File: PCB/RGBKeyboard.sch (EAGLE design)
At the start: 1 part, among them U1 MSP430F5529_PN_80

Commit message: USB lib and schematic
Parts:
- added C10, C11: 10 pF, rcl:C-USC0603K
- added C12: 4.7 uF, rcl:C-USC0603K
- added C4, C5: 32 pF, rcl:C-USC0603K
- added C6, C7: 220 nF, rcl:C-USC0603K
- added C8: 100 nF, rcl:C-USC0603K
- added C9: 10 uF, rcl:C-USC0603K
- added D2: BAS40, diode:BAS40
- added P2: 0475890001, MICRO_USB_B:0475890001
- added R5, R6, R7, R8: 27, rcl:R-US_R0603
- added R9: 1 M, rcl:R-US_R0603
- added S1: PTS645SM43SMTR, PTS645SM43SMTR:PTS645SM43SMTR
- added Y1: ECS-40-20-5PX-TR, ECS-40-20-5PX-TR:ECS-40-20-5PX-TR
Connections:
- removed net PU.0/DM: U1.PU.0/DP
- new net GND: C10.2, C11.2, C12.2, C4.2, C5.2, P2.GND, R9.1
- new net N$10: D2.C, P2.VCC
- new net N$4: R5.2, S1.P$1
- new net N$5: C8.2
- new net N$7: P2.ID
- new net N$8: P2.D-, R6.2
- new net N$9: P2.D+, R7.2
- new net PU.0/DP: C10.1, R7.1, R8.2, R9.2, U1.PU.0/DP
- new net V18: C7.1, U1.V18
- new net VBUS: C12.1, D2.A, U1.VBUS
- new net VSSU: C6.2, C7.2, C9.2, U1.VSSU
- new net VUSB: C6.1, C8.1, C9.1, S1.P$2, U1.VUSB
- new net XT2IN: C5.1, U1.P5.2/XT2IN, Y1.1
- new net XT2OUT: C4.1, U1.P5.3/XT2OUT, Y1.2
- net PU.1/DM: now also C11.1, R6.1
- net PUR: now also R5.1, R8.1

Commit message: Switches with LEDs and diodes
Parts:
- added D1, D10, D11, D12, D13, D3, D4, D5, D6, D7, D8, D9: BAV21W-7-F, BAV21W-7-F:BAV21W-7-F
- added U$1, U$10, U$11, U$12, U$2, U$3, U$4, U$5, U$6, U$7, U$8, U$9: CHERRY_MXCHERRY_MX_LED, CHERRY_MX:CHERRY_MXCHERRY_MX_LED
- added U10, U11, U12, U13, U2, U3, U4, U5, U6, U7, U8, U9: 3341, 3341:3341
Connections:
- new net +3V3: U10.VDD, U11.VDD, U12.VDD, U13.VDD, U2.VDD, U3.VDD, U4.VDD, U5.VDD, U6.VDD, U7.VDD, U8.VDD, U9.VDD
- new net CKO0: U5.CKO, U6.CKI
- new net CKO1: U10.CKI, U9.CKO
- new net COL0: U$1.2, U$3.2, U$9.2
- new net COL1: U$10.2, U$2.2, U$4.2
- new net COL2: U$11.2, U$5.2, U$7.2
- new net COL3: U$12.2, U$6.2, U$8.2
- new net N$1: D9.A, U$8.1
- new net N$11: D11.A, U$10.1
- new net N$12: D13.A, U$12.1
- new net N$13: U2.CKO, U3.CKI
- new net N$14: U2.SDO, U3.SDI
- new net N$15: U3.CKO, U4.CKI
- new net N$16: U3.SDO, U4.SDI
- new net N$17: U4.CKO, U5.CKI
- new net N$18: U4.SDO, U5.SDI
- new net N$19: U6.CKO, U7.CKI
- new net N$2: D5.A, U$4.1
- new net N$20: U6.SDO, U7.SDI
- new net N$21: U7.CKO, U8.CKI
- new net N$22: U7.SDO, U8.SDI
- new net N$23: U8.CKO, U9.CKI
- new net N$24: U8.SDO, U9.SDI
- new net N$25: U10.CKO, U11.CKI
- new net N$26: U10.SDO, U11.SDI
- new net N$27: U11.CKO, U12.CKI
- new net N$28: U11.SDO, U12.SDI
- new net N$29: U12.CKO, U13.CKI
- new net N$3: D7.A, U$6.1
- new net N$30: U12.SDO, U13.SDI
- new net N$6: D3.A, U$2.1
- new net ROW0: D1.A, D1.C, D3.C, D6.A, D6.C, D7.C, U$1.1, U$5.1
- new net ROW1: D4.A, D4.C, D5.C, D8.A, D8.C, D9.C, U$3.1, U$7.1
- new net ROW2: D10.A, D10.C, D11.C, D12.A, D12.C, D13.C, U$11.1, U$9.1
- new net SDO0: U5.SDO, U6.SDI
- new net SDO1: U10.SDI, U9.SDO
- new net UCA0CLK: U2.CKI
- new net UCA0SIMO: U2.SDI
- net GND: now also U10.GND, U11.GND, U12.GND, U13.GND, U2.GND, U3.GND, U4.GND, U5.GND, U6.GND, U7.GND, U8.GND, U9.GND

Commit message: Double check power and add headers
Power is sourced from USB through VBUS, goes through
internal LDO to VUSB and goes to DVCC.

Headers are for row/col debug and Spi-By-Wire
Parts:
- removed U$12: CHERRY_MXCHERRY_MX_LED, CHERRY_MX:CHERRY_MXCHERRY_MX_LED
- added C1, C2: 10 uF, rcl:C-USC0603K
- added C13: 470 nF, rcl:C-USC0603K
- added C14, C15, C3: 100 nF, rcl:C-USC0603K
- added D14: BAV21W-7-F, BAV21W-7-F:BAV21W-7-F
- added R1, R2, R3, R4: 4.7k, rcl:R-US_R0603
- added R10: 47 k, rcl:R-US_R0603
- added SV1, SV3: (no value), con-lstb:MA04-1
- added SV2: (no value), con-lstb:MA03-1
- added U$13: CHERRY_MX_LED, CHERRY_MX:CHERRY_MX_LED
- U$1, U$2, U$3, U$4, U$5, U$6, U$7, U$8, U$9: value CHERRY_MXCHERRY_MX_LED -> CHERRY_MX_LED; device CHERRY_MX:CHERRY_MXCHERRY_MX_LED -> CHERRY_MX:CHERRY_MX_LED
- U$10: value CHERRY_MXCHERRY_MX_LED -> CHERRY_MX_LEDCHERRY_MX_LED_1_2; device CHERRY_MX:CHERRY_MXCHERRY_MX_LED -> CHERRY_MX:CHERRY_MX_LEDCHERRY_MX_LED_1_2
- U$11: value CHERRY_MXCHERRY_MX_LED -> CHERRY_MX_LEDCHERRY_MX_LED_1_6; device CHERRY_MX:CHERRY_MXCHERRY_MX_LED -> CHERRY_MX:CHERRY_MX_LEDCHERRY_MX_LED_1_6
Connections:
- new net DVCC: C1.1, C14.1, C15.1, C2.1, C3.1, R10.1, U1.AVCC1, U1.DVCC1, U1.DVCC2, U1.VUSB
- new net N$31: C13.1, U1.VCORE
- new net N$32: D14.A, SV1.4
- new net N$33: U$3.2, U$4.2
- new net N$34: R10.2, U1.*RST/NMI/SBWTDIO
- new net N$35: U$7.2, U$8.2
- new net N$36: U$10.2, U$11.2
- new net RST: SV1.3
- new net TST: SV1.2
- net COL0: now also R1.2, SV3.4, U$13.2, U$2.2, U1.P1.3/TA0.2; no longer U$3.2, U$9.2
- net COL1: now also R2.2, SV3.3, U$5.2, U1.P1.4/TA0.3; no longer U$10.2, U$2.2
- net COL2: now also R3.2, SV3.2, U$6.2, U1.P1.5/TA0.4; no longer U$11.2, U$5.2
- net COL3: now also R4.2, SV3.1, U$10.2, U$9.2, U1.P1.6/TA1CLK/CBOUT; no longer U$12.2, U$6.2, U$8.2
- net GND: now also C1.2, C13.2, C14.2, C15.2, C2.2, C3.2, R1.1, R2.1, R3.1, R4.1, SV1.1, U1.AVSS1, U1.AVSS2, U1.DVSS1, U1.DVSS2
- net N$1: now also U$10.1; no longer U$8.1
- net N$10: now also D2.A; no longer D2.C
- net N$11: now also U$3.1; no longer U$10.1
- net N$12: now also U$11.1; no longer U$12.1
- net N$3: now also U$9.1; no longer U$6.1
- net N$6: now also U$5.1; no longer U$2.1
- net ROW0: now also SV2.3, U$13.1, U$6.1, U1.P1.0/TA0CLK/ACLK; no longer U$1.1, U$5.1
- net ROW1: now also SV2.2, U$1.1, U1.P1.1/TA0.0; no longer U$3.1
- net ROW2: now also SV2.1, U$2.1, U$8.1, U1.P1.2/TA0.1; no longer U$11.1, U$9.1
- net VBUS: now also D14.C, D2.C; no longer D2.A
- net VUSB: no longer U1.VUSB
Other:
- moved on the sheet: D2

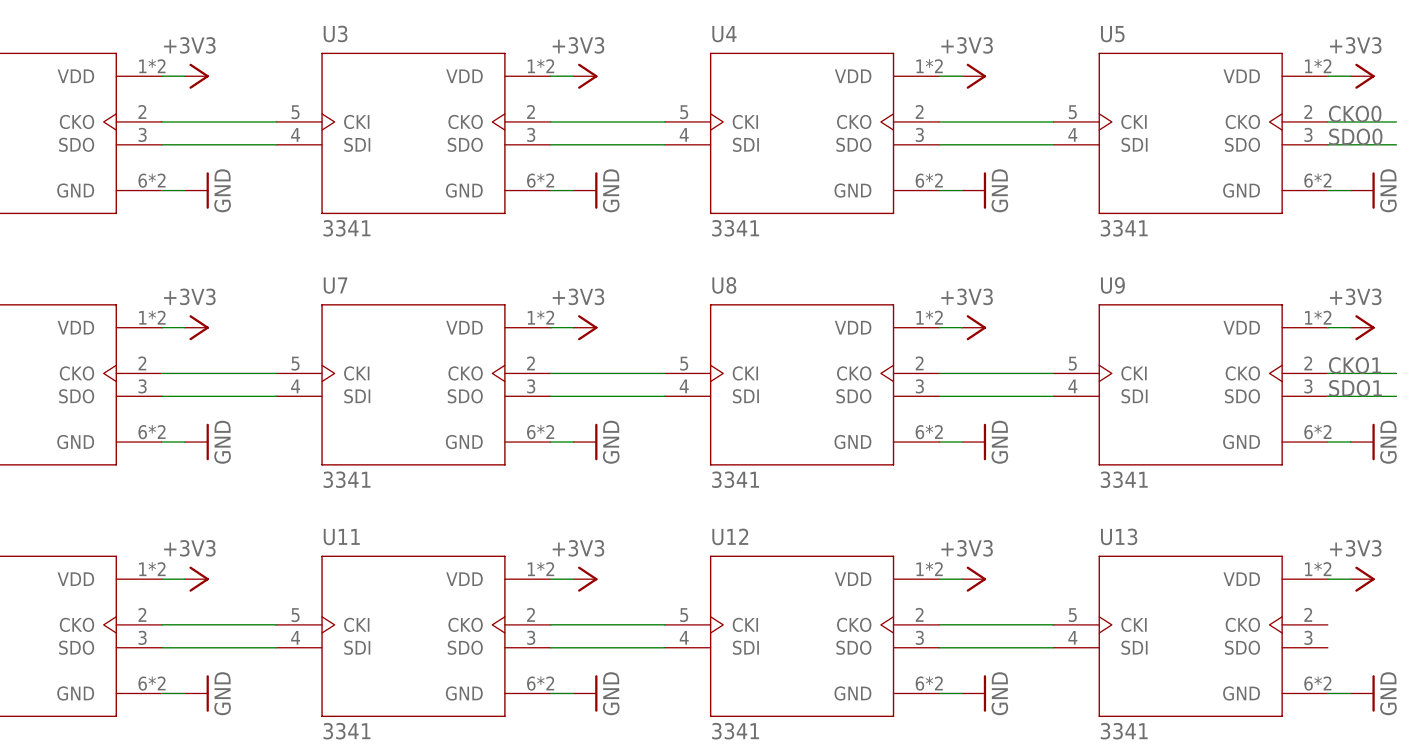
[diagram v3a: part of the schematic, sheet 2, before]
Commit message: Add power debug pins and double check connections
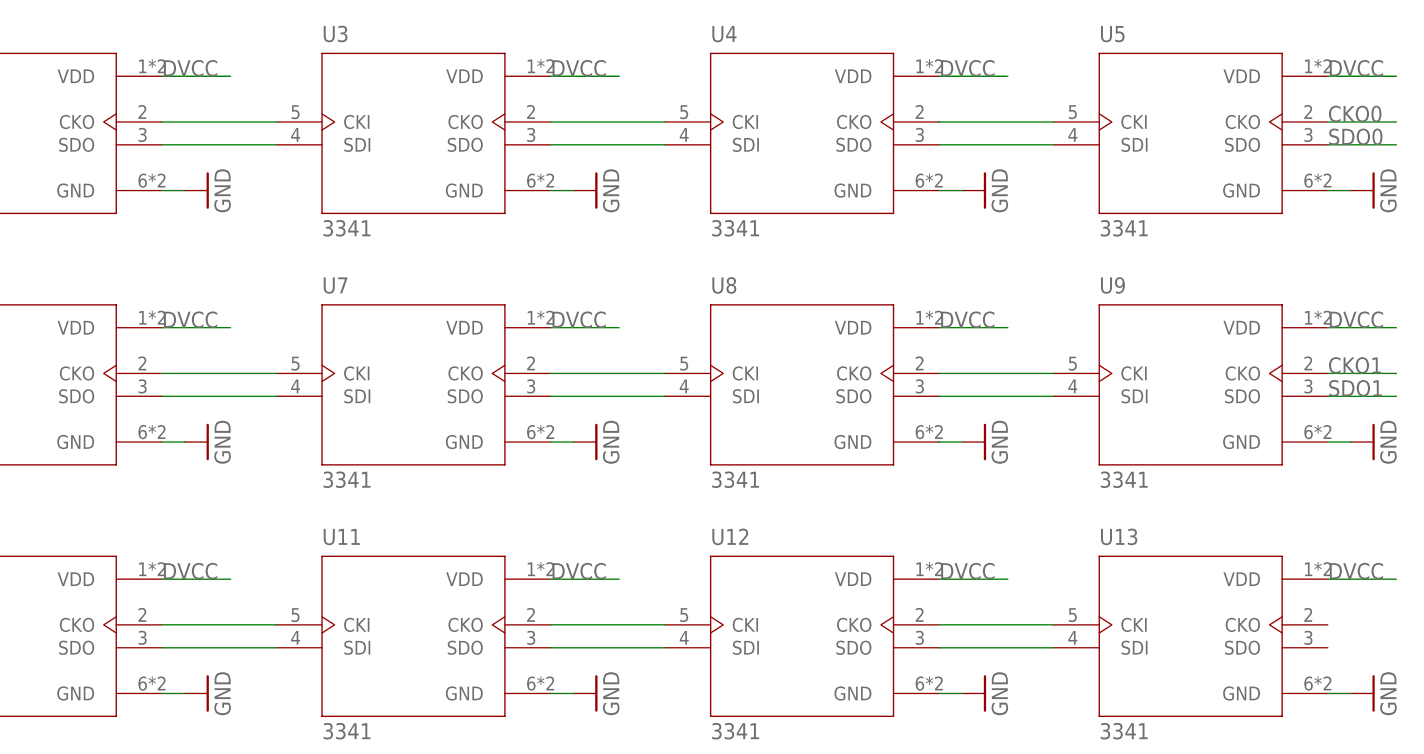
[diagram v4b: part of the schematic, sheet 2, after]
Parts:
- added SV4: (no value), con-lstb:MA03-1
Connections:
- removed net +3V3: U10.VDD, U11.VDD, U12.VDD, U13.VDD, U2.VDD, U3.VDD, U4.VDD, U5.VDD, U6.VDD, U7.VDD, U8.VDD, U9.VDD
- net DVCC: now also SV4.3, U10.VDD, U11.VDD, U12.VDD, U13.VDD, U2.VDD, U3.VDD, U4.VDD, U5.VDD, U6.VDD, U7.VDD, U8.VDD, U9.VDD
- net GND: now also SV4.2
- net UCA0CLK: now also U1.P2.7/UCB0STE/UCA0CLK
- net UCA0SIMO: now also U1.P3.3/UCA0TXD/UCA0SIMO

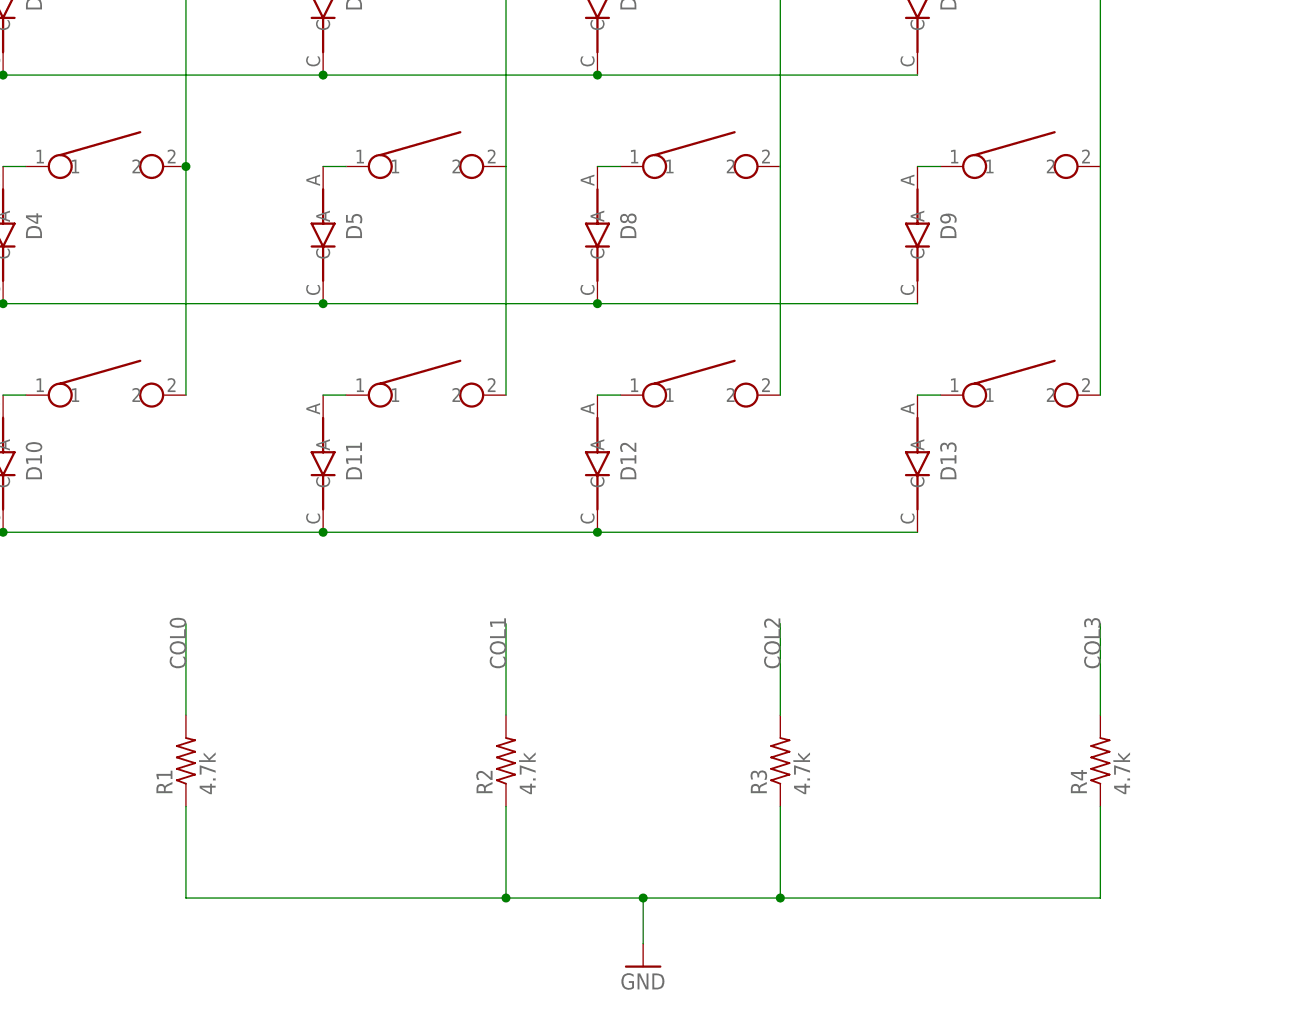
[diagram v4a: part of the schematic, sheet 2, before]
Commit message: Temp board and schematic (commit for progress)
Will be switching to a simpler design using the MSP430F5529
launchpad because the tools I have right now make it hard to
solder the MSP430 onto the board. Instead, the launchpad will
be connected to the board using header pins.
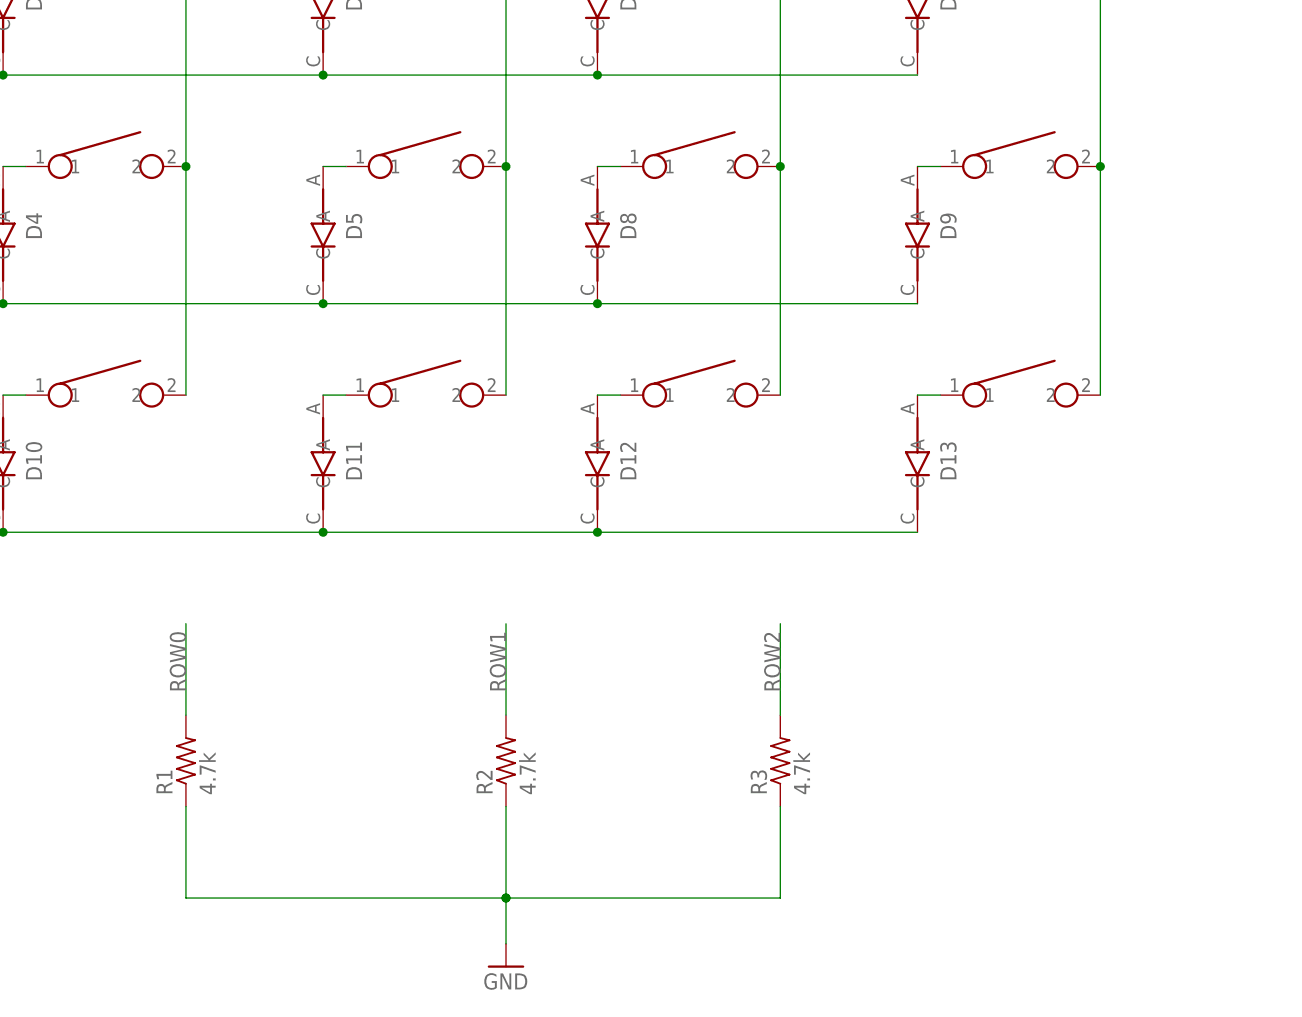
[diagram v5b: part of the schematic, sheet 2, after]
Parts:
- removed R4: 4.7k, rcl:R-US_R0603
- removed U$13: CHERRY_MX_LED, CHERRY_MX:CHERRY_MX_LED
- added U$12: CHERRY_MX, CHERRY_MX:CHERRY_MX
- R5: value 27 -> 100
- U$1, U$2, U$3, U$4, U$5, U$6, U$7, U$8, U$9: value CHERRY_MX_LED -> CHERRY_MX; device CHERRY_MX:CHERRY_MX_LED -> CHERRY_MX:CHERRY_MX
- U$10: value CHERRY_MX_LEDCHERRY_MX_LED_1_2 -> CHERRY_MXCHERRY_MX_1_2; device CHERRY_MX:CHERRY_MX_LEDCHERRY_MX_LED_1_2 -> CHERRY_MX:CHERRY_MXCHERRY_MX_1_2
- U$11: value CHERRY_MX_LEDCHERRY_MX_LED_1_6 -> CHERRY_MXCHERRY_MX_1_6; device CHERRY_MX:CHERRY_MX_LEDCHERRY_MX_LED_1_6 -> CHERRY_MX:CHERRY_MXCHERRY_MX_1_6
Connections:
- removed net N$34: R10.2, U1.*RST/NMI/SBWTDIO
- new net N$37: D10.A, U$3.1
- new net N$38: D1.A, U$1.1
- new net N$39: D4.A, U$2.1
- net COL0: now also U$3.2, U1.P1.6/TA1CLK/CBOUT; no longer R1.2, U$13.2, U1.P1.3/TA0.2
- net COL1: now also U$6.2, U1.P1.5/TA0.4; no longer R2.2, U1.P1.4/TA0.3
- net COL2: now also U$8.2, U$9.2, U1.P1.4/TA0.3; no longer R3.2, U$6.2, U1.P1.5/TA0.4
- net COL3: now also U$11.2, U$12.2, U1.P1.3/TA0.2; no longer R4.2, U$9.2, U1.P1.6/TA1CLK/CBOUT
- net GND: no longer R4.1
- net N$11: now also U$6.1; no longer U$3.1
- net N$2: now also U$5.1; no longer U$4.1
- net N$3: now also U$12.1; no longer U$9.1
- net N$33: now also D6.A, U$7.1; no longer U$3.2, U$4.2
- net N$35: now also D8.A, U$8.1; no longer U$7.2, U$8.2
- net N$36: now also D12.A, U$9.1; no longer U$10.2, U$11.2
- net N$6: now also U$4.1; no longer U$5.1
- net ROW0: now also R1.2, U1.P1.2/TA0.1; no longer D1.A, D6.A, U$13.1, U$6.1, U1.P1.0/TA0CLK/ACLK
- net ROW1: now also R2.2; no longer D4.A, D8.A, U$1.1, U$7.1
- net ROW2: now also R3.2, U1.P1.0/TA0CLK/ACLK; no longer D10.A, D12.A, U$2.1, U$8.1, U1.P1.2/TA0.1
- net RST: now also R10.2, U1.*RST/NMI/SBWTDIO

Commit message: Have a decent prototype but may switch LEDs
WS2812-2020s seem easier to solder but are harder to control.
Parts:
- removed C1, C2, C9: 10 uF, rcl:C-USC0603K
- removed C10, C11: 10 pF, rcl:C-USC0603K
- removed C12: 4.7 uF, rcl:C-USC0603K
- removed C13: 470 nF, rcl:C-USC0603K
- removed C14, C15, C3, C8: 100 nF, rcl:C-USC0603K
- removed C4, C5: 32 pF, rcl:C-USC0603K
- removed C6, C7: 220 nF, rcl:C-USC0603K
- removed P2: 0475890001, MICRO_USB_B:0475890001
- removed R10: 47 k, rcl:R-US_R0603
- removed R5: 100, rcl:R-US_R0603
- removed R6, R7, R8: 27, rcl:R-US_R0603
- removed R9: 1 M, rcl:R-US_R0603
- removed S1: PTS645SM43SMTR, PTS645SM43SMTR:PTS645SM43SMTR
- removed SV2: (no value), con-lstb:MA03-1
- removed Y1: ECS-40-20-5PX-TR, ECS-40-20-5PX-TR:ECS-40-20-5PX-TR
- added R4: 4.7k, rcl:R-US_R0603
- added SV5: (no value), con-lstb:MA03-1
- added U$13: CHERRY_MXCHERRY_MX_1_2, CHERRY_MX:CHERRY_MXCHERRY_MX_1_2
- added U$14: CHERRY_MXCHERRY_MX_1_6, CHERRY_MX:CHERRY_MXCHERRY_MX_1_6
- added U14: 3341, 3341:3341
- D2: value BAS40 -> BAV21W-7-F; device diode:BAS40 -> BAV21W-7-F:BAV21W-7-F
- U$10: value CHERRY_MXCHERRY_MX_1_2 -> CHERRY_MX; device CHERRY_MX:CHERRY_MXCHERRY_MX_1_2 -> CHERRY_MX:CHERRY_MX
- U$11: value CHERRY_MXCHERRY_MX_1_6 -> CHERRY_MX; device CHERRY_MX:CHERRY_MXCHERRY_MX_1_6 -> CHERRY_MX:CHERRY_MX
- U1: value MSP430F5529_PN_80 -> 3341; device MSP430F5529_80:MSP430F5529_PN_80 -> 3341:3341
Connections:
- removed net N$31: C13.1, U1.VCORE
- removed net N$32: D14.A, SV1.4
- removed net N$7: P2.ID
- removed net N$8: P2.D-, R6.2
- removed net PU.0/DP: C10.1, R7.1, R8.2, R9.2, U1.PU.0/DP
- removed net PU.1/DM: C11.1, R6.1, U1.PU.1/DM
- removed net PUR: R5.1, R8.1, U1.PUR
- removed net RST: R10.2, SV1.3, U1.*RST/NMI/SBWTDIO
- removed net TST: SV1.2
- removed net V18: C7.1, U1.V18
- removed net VBUS: C12.1, D14.C, D2.C, U1.VBUS
- removed net VSSU: C6.2, C7.2, C9.2, U1.VSSU
- removed net VUSB: C6.1, C8.1, C9.1, S1.P$2
- removed net XT2IN: C5.1, U1.P5.2/XT2IN, Y1.1
- removed net XT2OUT: C4.1, U1.P5.3/XT2OUT, Y1.2
- new net CKO2: U1.CKI, U13.CKO
- new net ROW3: D14.C, D2.C, R4.2, SV1.1
- new net SDO2: U1.SDI, U13.SDO
- net COL0: now also U$13.2; no longer U1.P1.6/TA1CLK/CBOUT
- net COL1: now also U$14.2; no longer U1.P1.5/TA0.4
- net COL2: no longer U1.P1.4/TA0.3
- net COL3: no longer U1.P1.3/TA0.2
- net DVCC: now also U1.VDD, U14.VDD; no longer C1.1, C14.1, C15.1, C2.1, C3.1, R10.1, U1.AVCC1, U1.DVCC1, U1.DVCC2, U1.VUSB
- net GND: now also R4.1, U1.GND, U14.GND; no longer C1.2, C10.2, C11.2, C12.2, C13.2, C14.2, C15.2, C2.2, C3.2, C4.2, C5.2, P2.GND, R9.1, SV1.1, U1.AVSS1, U1.AVSS2, U1.DVSS1, U1.DVSS2
- net N$10: now also U1.SDO, U14.SDI; no longer D2.A, P2.VCC
- net N$4: now also D2.A, U$13.1; no longer R5.2, S1.P$1
- net N$5: now also D14.A, U$14.1; no longer C8.2
- net N$9: now also U1.CKO, U14.CKI; no longer P2.D+, R7.2
- net ROW0: now also SV1.4; no longer SV2.3, U1.P1.2/TA0.1
- net ROW1: now also SV1.3; no longer SV2.2, U1.P1.1/TA0.0
- net ROW2: now also SV1.2; no longer SV2.1, U1.P1.0/TA0CLK/ACLK
- net UCA0CLK: now also SV5.3; no longer U1.P2.7/UCB0STE/UCA0CLK
- net UCA0SIMO: now also SV5.2; no longer U1.P3.3/UCA0TXD/UCA0SIMO
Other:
- moved on the sheet: R1, R2, R3, SV1
